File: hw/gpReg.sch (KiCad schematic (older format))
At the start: 7 parts, among them U501 74HC574, U502 74HC139, U503 74HC02, U504 74HC574, U505 74HC574, U506 74HC574, U507 74HC574

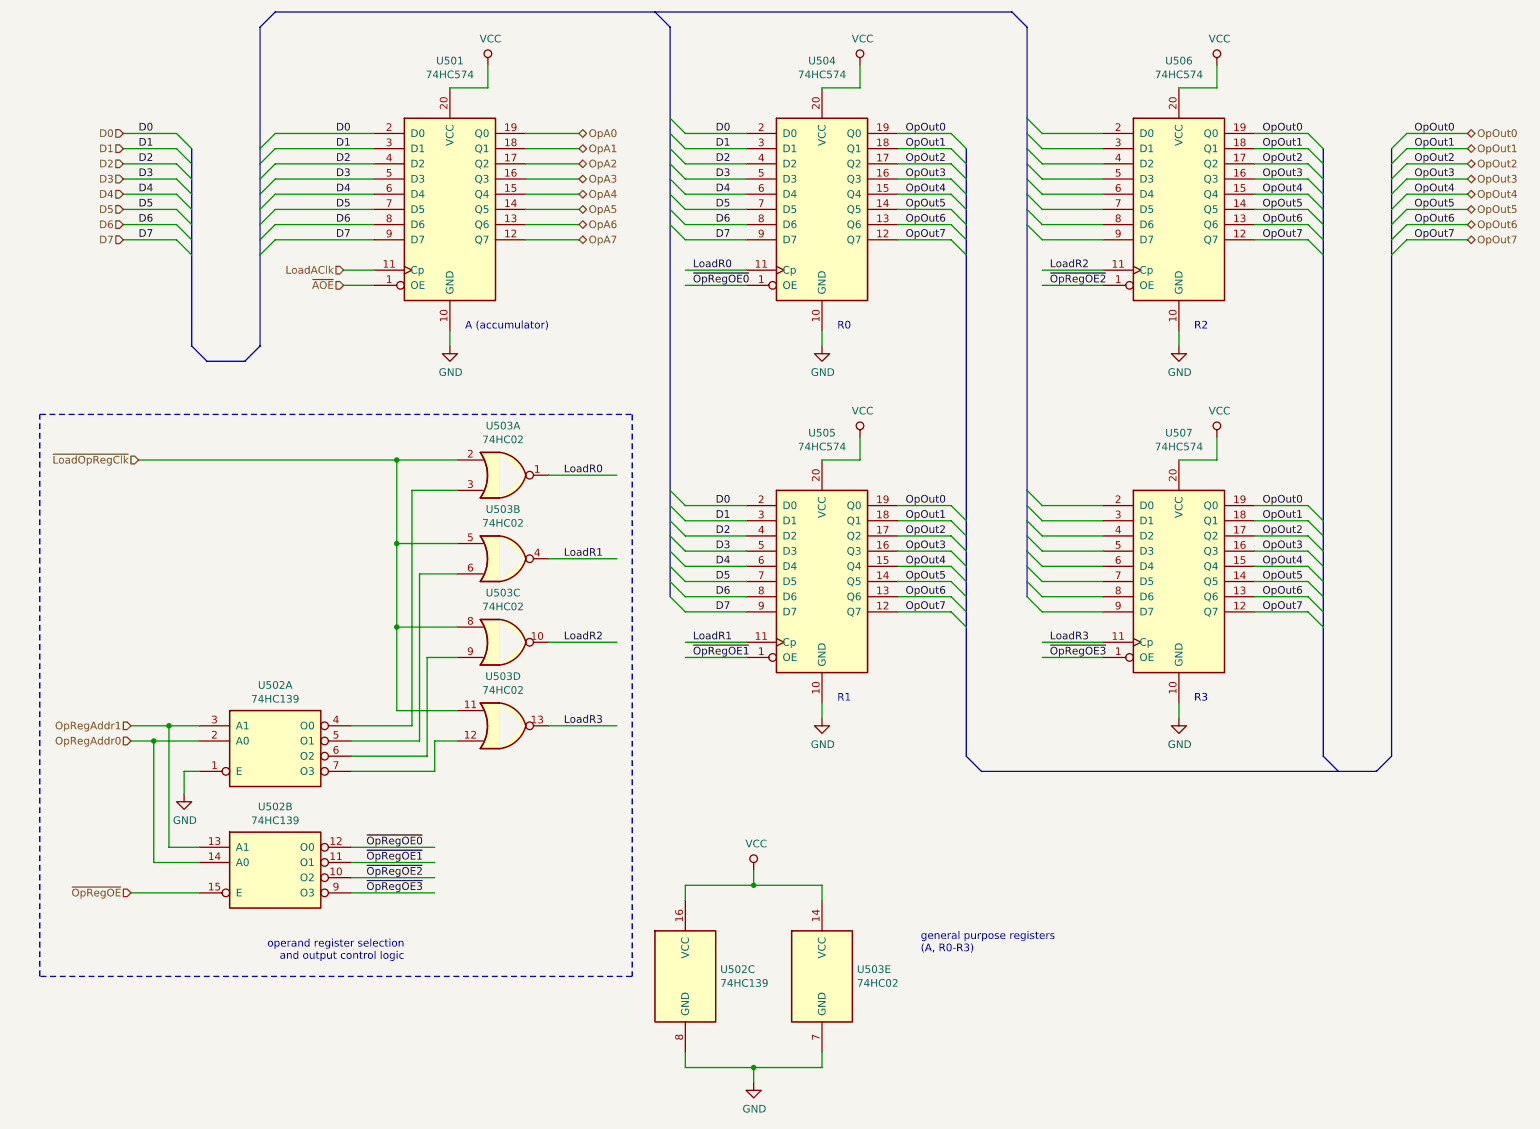
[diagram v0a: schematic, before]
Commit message: simplified GP regs slightly
An output enable signal for the operand registers
(R0-R3) is not necessary.  The address 0-3 selects
which one generates output.
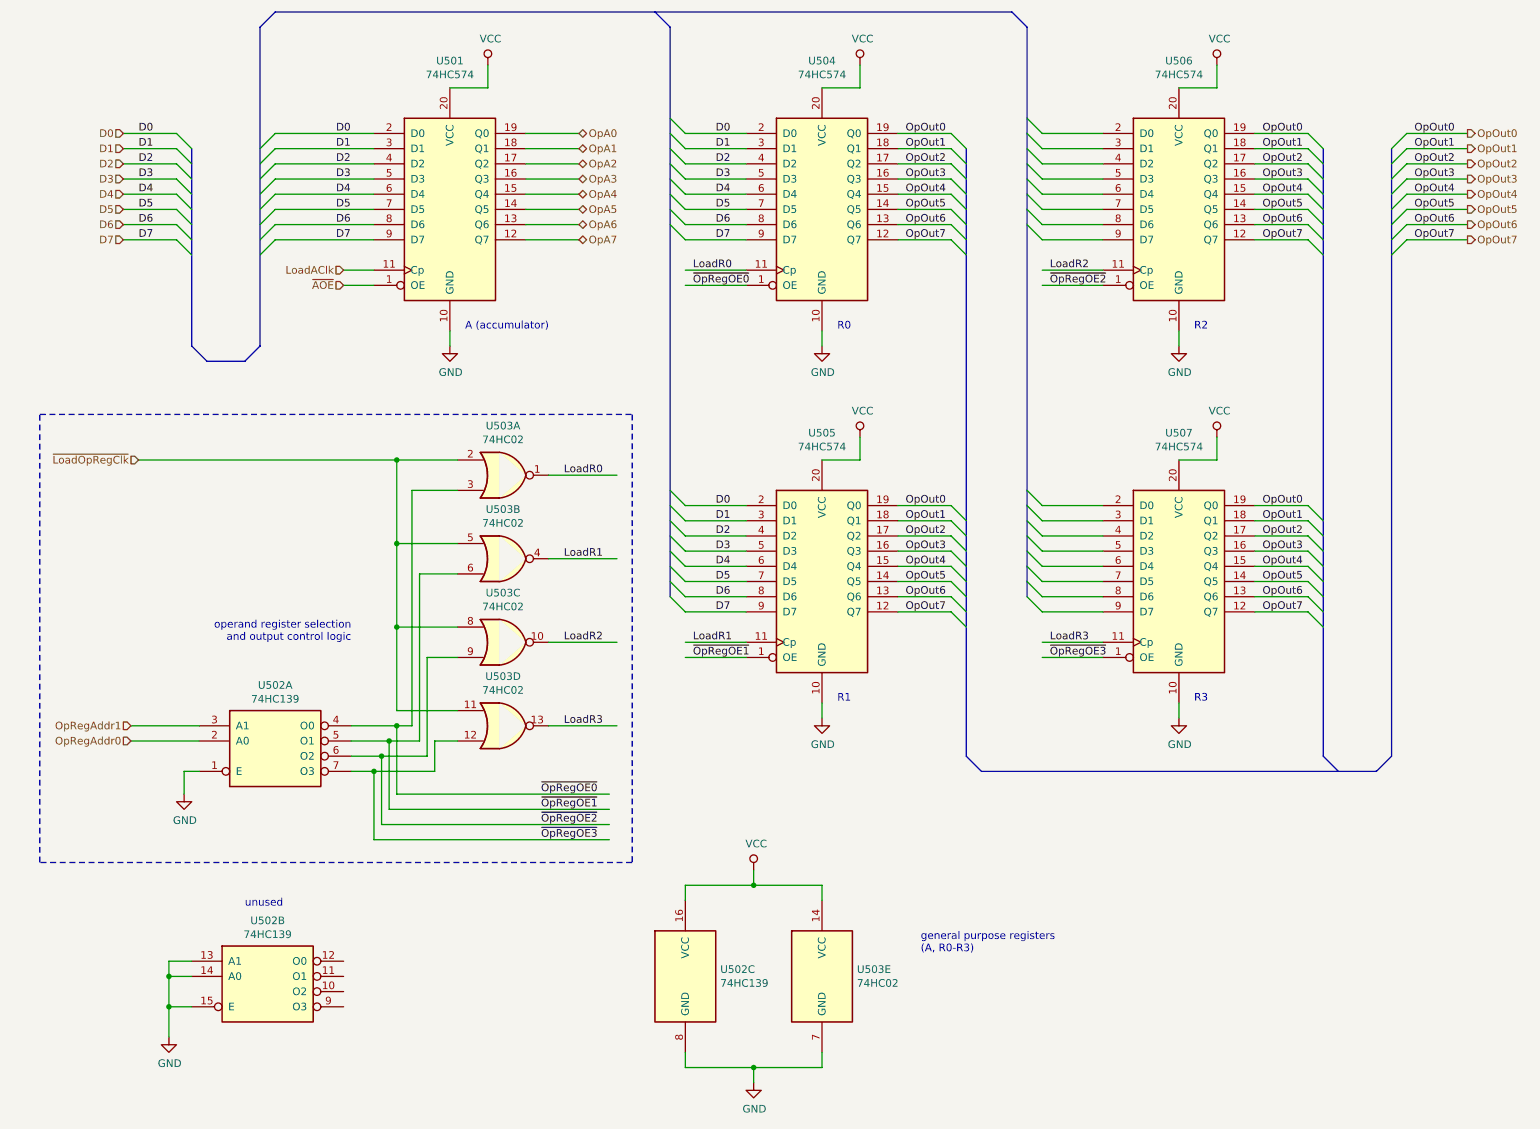
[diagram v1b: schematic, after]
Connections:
- net labels removed: ~OpRegOE
- wire segments 170 -> 177
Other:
- note added: "unused"
- moved on the sheet: U502B
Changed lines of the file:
@@
 L 74xx:74LS139 U502
 U 2 1 5DBE18D9
-P 2100 6400
-F 0 "U502" H 2100 6767 50  0000 C CNN
-F 1 "74HC139" H 2100 6676 50  0000 C CNN
-F 2 "" H 2100 6400 50  0001 C CNN
-F 3 "" H 2100 6400 50  0001 C CNN
-	2    2100 6400
+P 2050 7150
+F 0 "U502" H 2050 7517 50  0000 C CNN
+F 1 "74HC139" H 2050 7426 50  0000 C CNN
+F 2 "" H 2050 7150 50  0001 C CNN
+F 3 "" H 2050 7150 50  0001 C CNN
+	2    2050 7150
 	1    0    0    -1
 $EndComp
@@
 	1    0    0    -1
 $EndComp
-Wire Wire Line
-	1600 6600 1150 6600
-Text HLabel 1150 6600 0    50   Input ~ 0
-~OpRegOE
-Wire Wire Line
-	1600 5500 1400 5500
-Wire Wire Line
-	1600 5600 1300 5600
-Wire Wire Line
-	1600 6300 1400 6300
 Text HLabel 1150 5600 0    50   Input ~ 0
 OpRegAddr0
 Text HLabel 1150 5500 0    50   Input ~ 0
 OpRegAddr1
-Wire Wire Line
-	1400 6300 1400 5500
-Connection ~ 1400 5500
-Wire Wire Line
-	1400 5500 1150 5500
-Wire Wire Line
-	1300 6400 1300 5600
-Wire Wire Line
-	1300 6400 1600 6400
-Connection ~ 1300 5600
-Wire Wire Line
-	1300 5600 1150 5600
-Wire Wire Line
-	2600 6300 3150 6300
-Wire Wire Line
-	2600 6400 3150 6400
-Wire Wire Line
-	2600 6500 3150 6500
-Wire Wire Line
-	2600 6600 3150 6600
-Text Label 2700 6300 0    50   ~ 0
+Text Label 3850 5950 0    50   ~ 0
 ~OpRegOE0
-Text Label 2700 6400 0    50   ~ 0
+Text Label 3850 6050 0    50   ~ 0
 ~OpRegOE1
-Text Label 2700 6500 0    50   ~ 0
+Text Label 3850 6150 0    50   ~ 0
 ~OpRegOE2
-Text Label 2700 6600 0    50   ~ 0
+Text Label 3850 6250 0    50   ~ 0
 ~OpRegOE3
 Text Label 4850 2600 0    50   ~ 0
@@
 $EndComp
 Wire Wire Line
-	2600 5700 3100 5700
+	2600 5700 2800 5700
 Wire Wire Line
 	3100 5700 3100 5050
@@
 	3100 5050 3300 5050
 Wire Wire Line
-	2600 5600 3050 5600
+	2600 5600 2850 5600
 Wire Wire Line
 	3050 5600 3050 4500
@@
 	3050 4500 3300 4500
 Wire Wire Line
-	2600 5500 3000 5500
+	2600 5500 2900 5500
 Wire Wire Line
 	3000 5500 3000 3950
@@
 	7550 4950 7150 4950
 Wire Wire Line
-	2600 5800 3150 5800
+	2600 5800 2750 5800
 Wire Wire Line
 	3150 5800 3150 5600
@@
 Entry Wire Line
 	9450 2400 9550 2300
-Text HLabel 9950 1600 2    50   3State ~ 0
-OpOut0
-Text HLabel 9950 1700 2    50   3State ~ 0
-OpOut1
-Text HLabel 9950 1800 2    50   3State ~ 0
-OpOut2
-Text HLabel 9950 1900 2    50   3State ~ 0
-OpOut3
-Text HLabel 9950 2000 2    50   3State ~ 0
-OpOut4
-Text HLabel 9950 2100 2    50   3State ~ 0
-OpOut5
-Text HLabel 9950 2200 2    50   3State ~ 0
-OpOut6
-Text HLabel 9950 2300 2    50   3State ~ 0
-OpOut7
 Wire Notes Line
 	550  3450 4450 3450
 Wire Notes Line
-	4450 3450 4450 7150
+	4450 3450 4450 6400
 Wire Notes Line
-	4450 7150 550  7150
+	4450 6400 550  6400
 Wire Notes Line
-	550  7150 550  3450
-Text Notes 2950 7050 2    50   ~ 0
+	550  6400 550  3450
+Text Notes 2600 4950 2    50   ~ 0
 operand register selection\nand output control logic
 Wire Wire Line
@@
 Text Notes 3350 2900 0    50   ~ 0
 A (accumulator)
+Text HLabel 9950 1600 2    50   Output ~ 0
+OpOut0
+Text HLabel 9950 1700 2    50   Output ~ 0
+OpOut1
+Text HLabel 9950 1800 2    50   Output ~ 0
+OpOut2
+Text HLabel 9950 1900 2    50   Output ~ 0
+OpOut3
+Text HLabel 9950 2000 2    50   Output ~ 0
+OpOut4
+Text HLabel 9950 2100 2    50   Output ~ 0
+OpOut5
+Text HLabel 9950 2200 2    50   Output ~ 0
+OpOut6
+Text HLabel 9950 2300 2    50   Output ~ 0
+OpOut7
+Wire Wire Line
+	1150 5600 1600 5600
+Wire Wire Line
+	1150 5500 1600 5500
+Wire Wire Line
+	2900 5950 2900 5500
+Wire Wire Line
+	2900 5950 4300 5950
+Connection ~ 2900 5500
+Wire Wire Line
+	2900 5500 3000 5500
+Wire Wire Line
+	2850 6050 2850 5600
+Wire Wire Line
+	2850 6050 4300 6050
+Connection ~ 2850 5600
+Wire Wire Line
+	2850 5600 3050 5600
+Wire Wire Line
+	2800 6150 2800 5700
+Wire Wire Line
+	2800 6150 4300 6150
+Connection ~ 2800 5700
+Wire Wire Line
+	2800 5700 3100 5700
+Wire Wire Line
+	2750 6250 2750 5800
+Wire Wire Line
+	2750 6250 4300 6250
+Connection ~ 2750 5800
+Wire Wire Line
+	2750 5800 3150 5800
+Wire Wire Line
+	1550 7050 1400 7050
+Wire Wire Line
+	1400 7050 1400 7150
+Wire Wire Line
+	1550 7150 1400 7150
+Connection ~ 1400 7150
+Wire Wire Line
+	1400 7150 1400 7350
+Wire Wire Line
+	1550 7350 1400 7350
 Wire Bus Line
 	2100 800  6950 800
@@
 Wire Bus Line
 	6650 1700 6650 5700
+Connection ~ 1400 7350
+Wire Wire Line
+	1400 7350 1400 7550
+$Comp
+L power:GND #PWR?
+U 1 1 5DE8BE1E
+P 1400 7550
+F 0 "#PWR?" H 1400 7300 50  0001 C CNN
+F 1 "GND" H 1405 7377 50  0000 C CNN
+F 2 "" H 1400 7550 50  0001 C CNN
+F 3 "" H 1400 7550 50  0001 C CNN
+	1    1400 7550
+	1    0    0    -1
+$EndComp
+Text Notes 1900 6700 0    50   ~ 0
+unused
 $EndSCHEMATC
